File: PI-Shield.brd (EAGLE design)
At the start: 160 x 100 mm, 80 parts, among them IC1 PCF8574T, J10 T2I, J11 T2I, J12 T2I, J13 DF13-4P-1.25DSA, J14 DF13-4P-1.25DSA, J15 DF13-4P-1.25DSA, Q1 220mA/50V/3.5Ω, Q2 220mA/50V/3.5Ω, Q3 220mA/50V/3.5Ω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

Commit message: Board Update
Changes: [Reduced backplane connector from 26->12 positions, added board outline matching last year's, placement of components]
To Do: [Routing, which should be done within next 24 hrs :P]
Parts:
- U$3: value IPL_13X2 -> 6X_CONN; device PI-SHIELD, Solenoid-Backplane:IPL13X2 -> PI-SHIELD, Solenoid-Backplane:IPL6X2
- moved J1 189.3 mm to (67.4, 35.4), turned to 90 degrees
- moved R22 181.9 mm to (34.2, 7.75), turned to 270 degrees
- moved R20 178.4 mm to (46.4, 20.3), flipped to the bottom, turned to 180 degrees
- moved R21 168.4 mm to (17.4, 4.32)
- moved U$8 167.5 mm to (65.9, 3.94), turned to 90 degrees
- moved U3 167.1 mm to (50.5, 10.7), turned to 270 degrees
- moved C10 165.4 mm to (18.0, 12.1), turned to 90 degrees
- moved R15 161.7 mm to (43.8, 18.8), flipped to the bottom
- moved R18 161.6 mm to (17.4, 2.29)
- moved J13 158.7 mm to (61.7, 49.9), turned to 180 degrees
- moved C8 158.3 mm to (21.5, 18.3), flipped to the bottom
- moved C9 157.7 mm to (21.3, 24.5), flipped to the bottom, turned to 180 degrees
- moved J14 157.4 mm to (43.9, 49.9), turned to 180 degrees
- moved R17 155.1 mm to (27.4, 18.5), flipped to the bottom, turned to 180 degrees
- moved R12 153.6 mm to (41.3, 14.7), flipped to the bottom, turned to 90 degrees
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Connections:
- removed net ALERT1: U$3.17
- removed net ALERT2: U$3.19
- removed net C2_1: U$3.21
- removed net C2_2: U$3.22
- removed net DATA: U$3.25
- removed net SWCLK: U$3.11
- removed net SWDIO: U$3.13
- new net N$5: U$3.4
- net +3V3: now also U$3.12; no longer U$3.1
- net 5V: now also U$3.8; no longer U$3.3
- net CAN_H: no longer U$3.24
- net CAN_L: no longer U$3.26
- net CLK: no longer U$3.23
- net GND: now also U$3.10; no longer U$3.15, U$3.20, U$3.4, U$3.5, U$3.7, U$3.9
- net SOL1_1: now also U$3.1; no longer U$3.8
- net SOL2_1: now also U$3.3; no longer U$3.10
- net SOL3_1: now also U$3.5; no longer U$3.12
- net SOL4_1: now also U$3.7; no longer U$3.14
- net SOL5_1: now also U$3.9; no longer U$3.16
- net SOL6_1: now also U$3.11; no longer U$3.18
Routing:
- added copper zone on layer 1, net GND
- added copper zone on layer 16, net GND
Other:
- board size 160 x 100 mm -> 69.8 x 73 mm

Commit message: Schematic Update
Changes: [FREAKING FORGOT TO LABEL A PIN >:((((]
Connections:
- removed net N$5: U$3.4
- net 12V: now also U$3.4
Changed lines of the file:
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@@
 <contactref element="C15" pad="+"/>
 <contactref element="U$3" pad="2"/>
+<contactref element="U$3" pad="4"/>
 <wire x1="46.101" y1="8.193" x2="45.606" y2="18.288" width="0" layer="19" extent="1-1"/>
-<wire x1="44.45" y1="2.667" x2="46.101" y2="8.193" width="0" layer="19" extent="1-1"/>
+<wire x1="46.99" y1="2.667" x2="46.101" y2="8.193" width="0" layer="19" extent="1-1"/>
+<wire x1="44.45" y1="2.667" x2="46.99" y2="2.667" width="0" layer="19" extent="1-1"/>
 </signal>
 <signal name="SOL1_1">
@@
 <wire x1="58.801" y1="19.84" x2="57.15" y2="2.667" width="0" layer="19" extent="16-16"/>
 </signal>
-<signal name="N$5">
-<contactref element="U$3" pad="4"/>
-</signal>
 </signals>

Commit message: Routing Hard >:(
Changes: [Started routing,,,,, it's going well???? i dunno, *power polygons*]
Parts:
- moved U$3 12.5 mm to (50.0, -8.51)
- moved J5 3.82 mm to (67.6, 61.6)
- moved U$6 2.74 mm to (40.0, 2.67)
- moved J7 2.55 mm to (62.7, 38.0), turned to 270 degrees
- moved D1 1.37 mm to (30.7, 43.4)
- moved C12 1.08 mm to (31.0, 39.1)
- moved C4 1.08 mm to (24.9, 43.2)
- moved R1 1.08 mm to (26.5, 43.2)
- moved R10 1.08 mm to (21.5, 40.1)
- moved U2 1.08 mm to (25.3, 37.0)
- moved J1 1.02 mm to (66.4, 35.4)
- moved R2 0.92 mm to (29.0, 43.2), turned to 270 degrees
- moved R5 0.92 mm to (32.3, 70.2)
- moved C11 0.80 mm to (31.0, 35.3)
- moved D4 0.80 mm to (30.2, 17.0)
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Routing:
- net 3V3: track 0.00 -> 142.6 mm, vias 0 -> 2
- net 5V: track 0.00 -> 105.4 mm, vias 0 -> 1
- net CAN_L: track 0.00 -> 43.0 mm, vias 0 -> 1
- net CAN_H: track 0.00 -> 43.0 mm, vias 0 -> 1
- net PWM: track 0.00 -> 41.7 mm
- net PI_POWER: track 0.00 -> 25.8 mm
- net SDA_ADC: track 0.00 -> 17.2 mm
- net AMP_OUT: track 0.00 -> 16.3 mm, vias 0 -> 1
- net CLK: track 0.00 -> 16.2 mm
- net TXCAN: track 0.00 -> 16.1 mm, vias 0 -> 1
- net MISO: track 0.00 -> 15.7 mm
- net INT: track 0.00 -> 15.1 mm
- net RX: track 0.00 -> 14.9 mm
- net TX: track 0.00 -> 14.3 mm
- net RXCAN: track 0.00 -> 14.3 mm, vias 0 -> 1
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- added copper zone on layer 1, net 5V
- added copper zone on layer 1, net 5V_RAW
- added copper zone on layer 1, net PI_POWER

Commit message: Routing :)
Change: [bro why this game of flow so hard??]
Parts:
- moved C15 23.7 mm to (65.5, 34.3), turned to 270 degrees
- moved U$3 19.1 mm to (58.2, 8.76), turned to 180 degrees
- moved U3 15.1 mm to (62.0, 20.6), flipped to the bottom, turned to 180 degrees
- moved R20 8.62 mm to (48.4, 28.7)
- moved R9 8.07 mm to (46.6, 31.0)
- moved R8 8.02 mm to (48.3, 33.4)
- moved C13 7.58 mm to (45.0, 37.8)
- moved J6 7.55 mm to (40.8, 56.5), turned to 180 degrees
- moved J1 7.37 mm to (66.4, 42.8)
- moved J7 7.37 mm to (62.7, 45.3)
- moved R12 4.34 mm to (45.5, 15.9), turned to 0 degrees
- moved U$6 3.61 mm to (37.7, 5.46), turned to 90 degrees
- moved U$4 3.45 mm to (35.3, 47.8)
- moved U$5 3.45 mm to (40.5, 47.1)
- moved IC1 3.41 mm to (57.4, 16.8), flipped to the top, turned to 90 degrees
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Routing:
- net SDA: track 13.4 -> 137.7 mm, vias 0 -> 7
- net SCL: track 12.9 -> 130.3 mm, vias 0 -> 6
- net A_INT: track 0.00 -> 66.6 mm
- net 5V: track 105.4 -> 168.0 mm, vias 1 -> 4
- net 3V3: track 142.6 -> 201.6 mm, vias 2 -> 3
- net !AMP_RESET: track 0.00 -> 53.1 mm, vias 0 -> 1
- net IMU_INT: track 7.53 -> 59.5 mm, vias 0 -> 1
- net SOL6_1: track 0.00 -> 47.8 mm
- net SOL5_1: track 0.00 -> 42.0 mm
- net 12V: track 0.00 -> 37.8 mm, vias 0 -> 1
- net SOL4_1: track 0.00 -> 37.3 mm
- net SOL3_1: track 0.00 -> 31.8 mm
- net IMU_RESET: track 0.00 -> 30.9 mm
- net SOL2_1: track 0.00 -> 26.9 mm
- net MOSI: track 13.7 -> 37.2 mm
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
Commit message: Fixed Like 2 Routes smh
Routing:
- net SCL: track 130.3 -> 137.4 mm
- net SDA: track 137.7 -> 142.7 mm
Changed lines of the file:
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@@
 <layer number="43" name="vRestrict" color="2" fill="10" visible="yes" active="yes"/>
 <layer number="44" name="Drills" color="7" fill="1" visible="no" active="yes"/>
-<layer number="45" name="Holes" color="7" fill="1" visible="no" active="yes"/>
+<layer number="45" name="Holes" color="7" fill="1" visible="yes" active="yes"/>
 <layer number="46" name="Milling" color="3" fill="1" visible="no" active="yes"/>
 <layer number="47" name="Measures" color="7" fill="1" visible="no" active="yes"/>
@@
 <wire x1="61.468" y1="47.498" x2="66.04" y2="47.498" width="0.254" layer="16"/>
 <wire x1="66.04" y1="47.498" x2="66.421" y2="47.879" width="0.254" layer="16"/>
-<wire x1="50.546" y1="41.91" x2="49.022" y2="40.386" width="0.254" layer="1"/>
+<wire x1="50.038" y1="41.402" x2="49.022" y2="40.386" width="0.254" layer="1"/>
 <wire x1="49.022" y1="40.386" x2="49.022" y2="39.624" width="0.254" layer="1"/>
 <via x="49.022" y="39.624" extent="1-16" drill="0.35"/>
 <wire x1="49.022" y1="39.624" x2="49.022" y2="33.489" width="0.254" layer="16"/>
 <wire x1="49.022" y1="33.489" x2="49.11" y2="33.401" width="0.254" layer="16"/>
-<wire x1="50.546" y1="45.212" x2="45.847" y2="49.911" width="0.254" layer="1"/>
-<wire x1="43.805" y1="49.911" x2="45.847" y2="49.911" width="0.254" layer="1"/>
-<wire x1="50.546" y1="45.212" x2="50.546" y2="41.91" width="0.254" layer="1"/>
+<wire x1="43.805" y1="49.911" x2="43.805" y2="49.159" width="0.254" layer="1"/>
+<wire x1="50.038" y1="42.926" x2="43.805" y2="49.159" width="0.254" layer="1"/>
+<wire x1="50.038" y1="42.926" x2="50.038" y2="41.402" width="0.254" layer="1"/>
 <wire x1="14.1732" y1="14.8336" x2="15.3416" y2="14.8336" width="0.254" layer="1"/>
 <wire x1="15.3416" y1="14.8336" x2="18.796" y2="18.288" width="0.254" layer="1"/>
@@
 <wire x1="41.574" y1="13.97" x2="42.926" y2="13.97" width="0.254" layer="16"/>
 <via x="42.926" y="13.97" extent="1-16" drill="0.35"/>
-<wire x1="45.72" y1="13.462" x2="43.434" y2="13.462" width="0.254" layer="1"/>
+<wire x1="43.434" y1="13.462" x2="45.72" y2="13.462" width="0.254" layer="1"/>
 <wire x1="42.926" y1="13.97" x2="43.434" y2="13.462" width="0.254" layer="1"/>
-<wire x1="45.72" y1="13.462" x2="45.974" y2="13.716" width="0.254" layer="1"/>
-<via x="45.974" y="13.716" extent="1-16" drill="0.35"/>
 <wire x1="46.482" y1="15.709" x2="46.482" y2="14.224" width="0.254" layer="16"/>
-<wire x1="45.974" y1="13.716" x2="46.482" y2="14.224" width="0.254" layer="16"/>
 <wire x1="46.316" y1="15.875" x2="46.482" y2="15.709" width="0.254" layer="16"/>
-<wire x1="45.974" y1="13.716" x2="52.804" y2="13.589" width="0" layer="19" extent="1-1"/>
+<wire x1="52.804" y1="13.589" x2="47.117" y2="13.589" width="0.254" layer="1"/>
+<wire x1="47.117" y1="13.589" x2="46.482" y2="14.224" width="0.254" layer="1"/>
+<via x="46.482" y="14.224" extent="1-16" drill="0.35"/>
+<wire x1="45.72" y1="13.462" x2="46.482" y2="14.224" width="0.254" layer="1"/>
 </signal>
 <signal name="SCL">
@@
 <wire x1="46.228" y1="36.83" x2="46.228" y2="36.322" width="0.254" layer="1"/>
 <via x="46.228" y="36.322" extent="1-16" drill="0.35"/>
-<wire x1="47.752" y1="45.72" x2="43.561" y2="49.911" width="0.254" layer="1"/>
-<wire x1="42.555" y1="49.911" x2="43.561" y2="49.911" width="0.254" layer="1"/>
-<wire x1="47.752" y1="45.72" x2="47.752" y2="38.354" width="0.254" layer="1"/>
+<wire x1="47.752" y1="43.434" x2="42.555" y2="48.631" width="0.254" layer="1"/>
+<wire x1="42.555" y1="49.911" x2="42.555" y2="48.631" width="0.254" layer="1"/>
+<wire x1="47.752" y1="43.434" x2="47.752" y2="38.354" width="0.254" layer="1"/>
 <wire x1="46.228" y1="34.544" x2="45.72" y2="34.036" width="0.254" layer="16"/>
 <wire x1="45.72" y1="34.036" x2="45.72" y2="31.027" width="0.254" layer="16"/>
@@
 <wire x1="46.228" y1="17.526" x2="46.4625" y2="17.7605" width="0.254" layer="16"/>
 <wire x1="46.4625" y1="17.7605" x2="46.4625" y2="19.5775" width="0.254" layer="16"/>
-<wire x1="46.228" y1="17.526" x2="52.804" y2="14.859" width="0" layer="19" extent="1-1"/>
+<wire x1="46.228" y1="17.526" x2="47.498" y2="17.526" width="0.254" layer="1"/>
+<wire x1="50.165" y1="14.859" x2="52.804" y2="14.859" width="0.254" layer="1"/>
+<wire x1="47.498" y1="17.526" x2="50.165" y2="14.859" width="0.254" layer="1"/>
 <wire x1="41.91" y1="29.972" x2="41.783" y2="29.972" width="0" layer="19" extent="16-16"/>
 </signal>

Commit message: Update PI-Shield.brd
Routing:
- net 5V: track 168.0 -> 171.4 mm, vias 4 -> 5
- net PI_POWER: track 25.8 -> 27.1 mm
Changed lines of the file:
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@@
 <wire x1="34.544" y1="9.906" x2="34.036" y2="9.906" width="0.635" layer="1"/>
 <wire x1="47.244" y1="6.223" x2="36.703" y2="6.223" width="0.635" layer="1"/>
+<via x="27.94" y="12.954" extent="1-16" drill="0.35"/>
+<wire x1="25.9748" y1="15.428" x2="26.9644" y2="14.4384" width="0.508" layer="16"/>
+<wire x1="26.9644" y1="14.4384" x2="26.9644" y2="13.6556625" width="0.508" layer="16"/>
+<wire x1="27.94" y1="12.954" x2="27.6660625" y2="12.954" width="0.508" layer="16"/>
+<wire x1="27.6660625" y1="12.954" x2="26.9644" y2="13.6556625" width="0.508" layer="16"/>
 <wire x1="18.249" y1="2.286" x2="18.288" y2="1.4732" width="0" layer="19" extent="1-16"/>
-<wire x1="25.8748" y1="15.328" x2="26.924" y2="11.684" width="0" layer="19" extent="1-16"/>
 </signal>
 <signal name="RX0_INT">
@@
 <wire x1="8.1846" y1="8.845" x2="11.6332" y2="12.2936" width="1.778" layer="1"/>
 <wire x1="11.6332" y1="12.2936" x2="11.6332" y2="14.8336" width="1.778" layer="1"/>
-<wire x1="4.191" y1="8.845" x2="9.734" y2="3.302" width="1.778" layer="1"/>
-<wire x1="9.734" y1="3.302" x2="14.224" y2="3.302" width="1.778" layer="1"/>
+<wire x1="7.448" y1="3.302" x2="4.191" y2="6.559" width="1.778" layer="1"/>
+<wire x1="4.191" y1="8.845" x2="4.191" y2="6.559" width="1.778" layer="1"/>
+<wire x1="7.448" y1="3.302" x2="14.224" y2="3.302" width="1.778" layer="1"/>
 <polygon width="0.1524" layer="1">
 <vertex x="13.97" y="5.334"/>
@@
 <wire x1="57.023" y1="4.064" x2="62.8396" y2="4.064" width="0.3048" layer="16"/>
 <wire x1="62.8396" y1="4.064" x2="65.786" y2="7.0104" width="0.3048" layer="16"/>
-<wire x1="65.786" y1="7.0104" x2="65.786" y2="15.748" width="0.3048" layer="16"/>
-<wire x1="65.786" y1="15.748" x2="65.405" y2="16.129" width="0.3048" layer="16"/>
-<wire x1="65.405" y1="16.129" x2="64.451" y2="16.129" width="0.3048" layer="16"/>
+<wire x1="65.786" y1="7.0104" x2="65.786" y2="15.494" width="0.3048" layer="16"/>
+<wire x1="65.786" y1="15.494" x2="65.151" y2="16.129" width="0.3048" layer="16"/>
+<wire x1="65.151" y1="16.129" x2="64.451" y2="16.129" width="0.3048" layer="16"/>
 </signal>
 <signal name="SOL2_1">

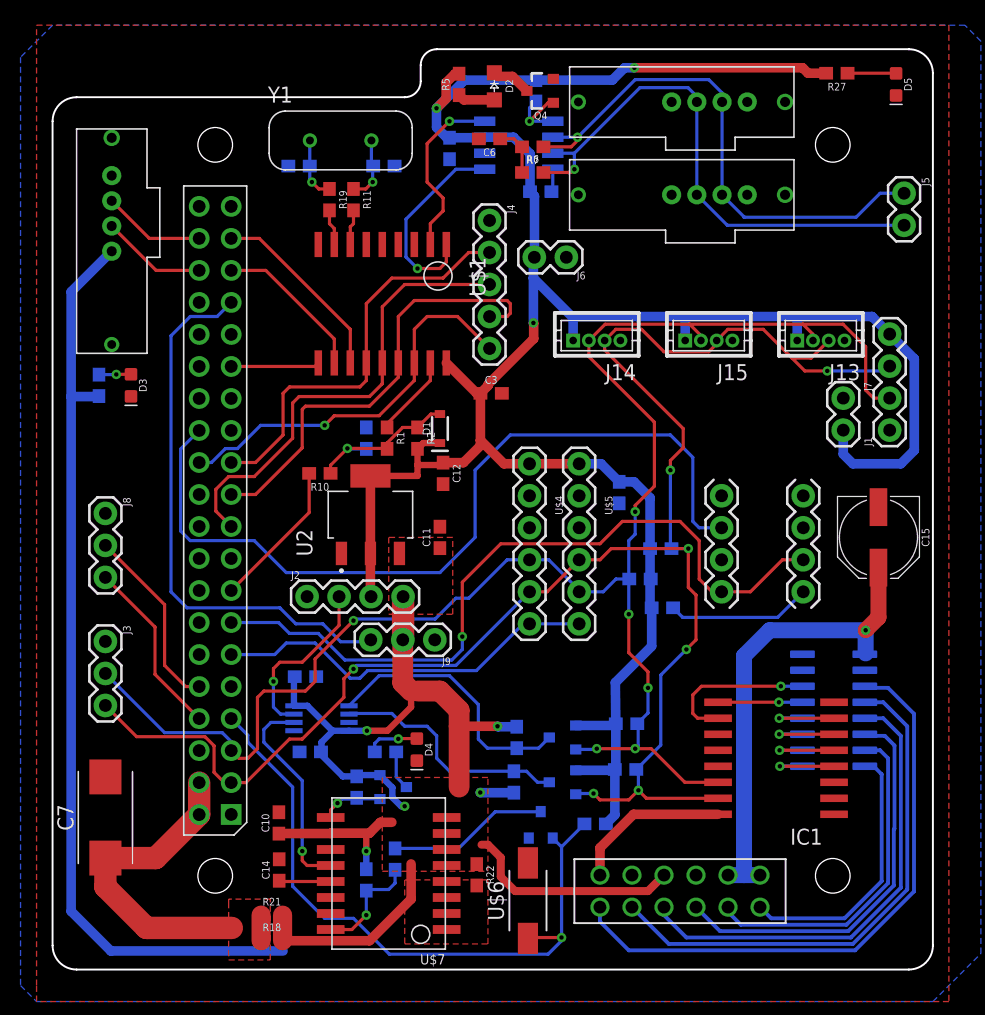
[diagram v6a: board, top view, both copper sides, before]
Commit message: Alumni Design Updates
Changes: [Trace Matched SCL/SDA & TX/RX, added alumni feedback]
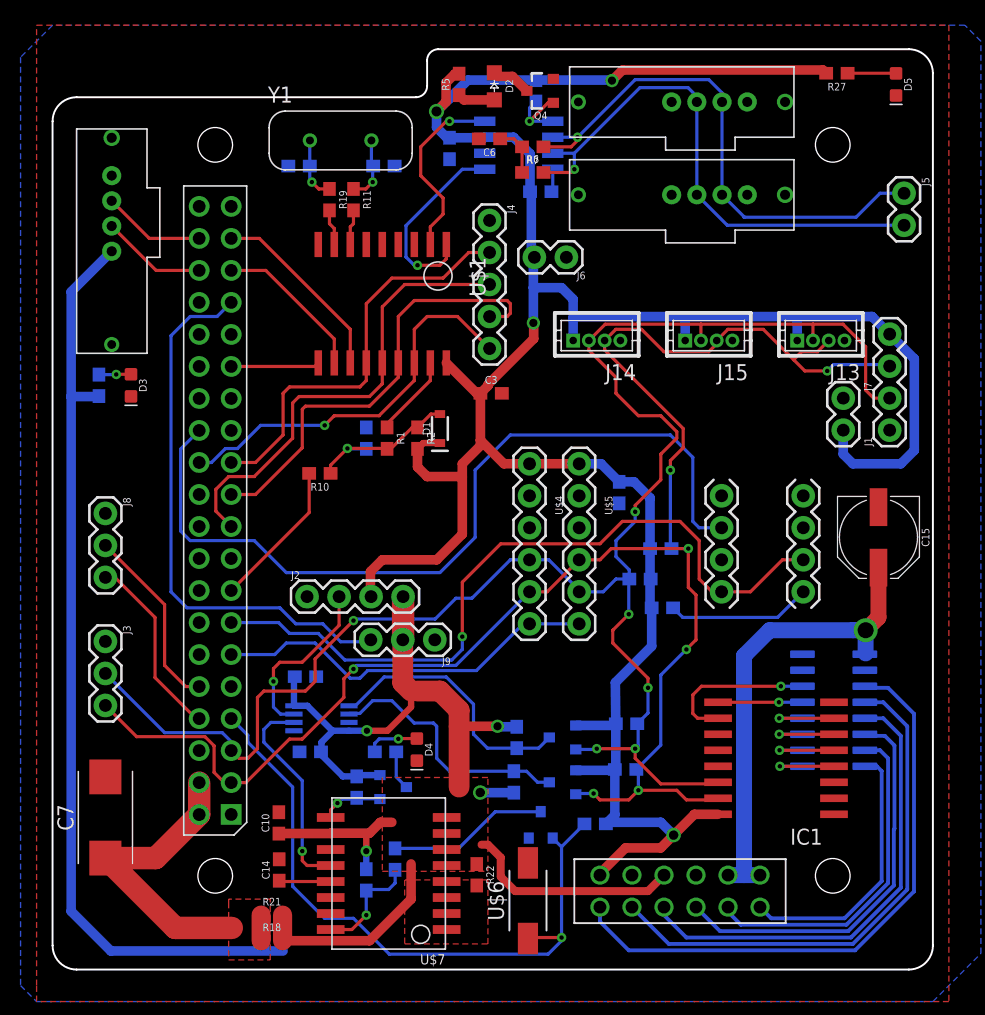
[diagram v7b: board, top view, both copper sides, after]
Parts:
- removed C11, C12: 4.7uF, SparkFun-Capacitors:0603
- removed U2: AZ1117EH-3.3TRG1, AZ1117EH-3.3TRG1:SOT230P700X180-4N
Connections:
- removed net +3V3: IC1.16, U$3.12
- net 3V3: now also IC1.16, U$3.12; no longer C12.1, U2.2, U2.4
- net 5V: no longer C11.1, U2.3
- net GND: no longer C11.2, C12.2, U2.1
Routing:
- net 3V3: track 201.6 -> 221.7 mm, vias 3 -> 4
- net +3V3: track 12.6 -> 0.00 mm
- net SCL: track 137.4 -> 142.7 mm
- net 5V: track 171.4 -> 168.0 mm, vias 5 -> 4
- net PI_POWER: track 27.1 -> 25.8 mm
- net SDA_ADC: track 19.8 -> 21.1 mm
- net RXCAN: track 14.3 -> 15.2 mm
- net TXCAN: track 16.1 -> 15.4 mm
- net TX: track 14.3 -> 14.9 mm
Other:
- outline, holes or cut-outs redrawn

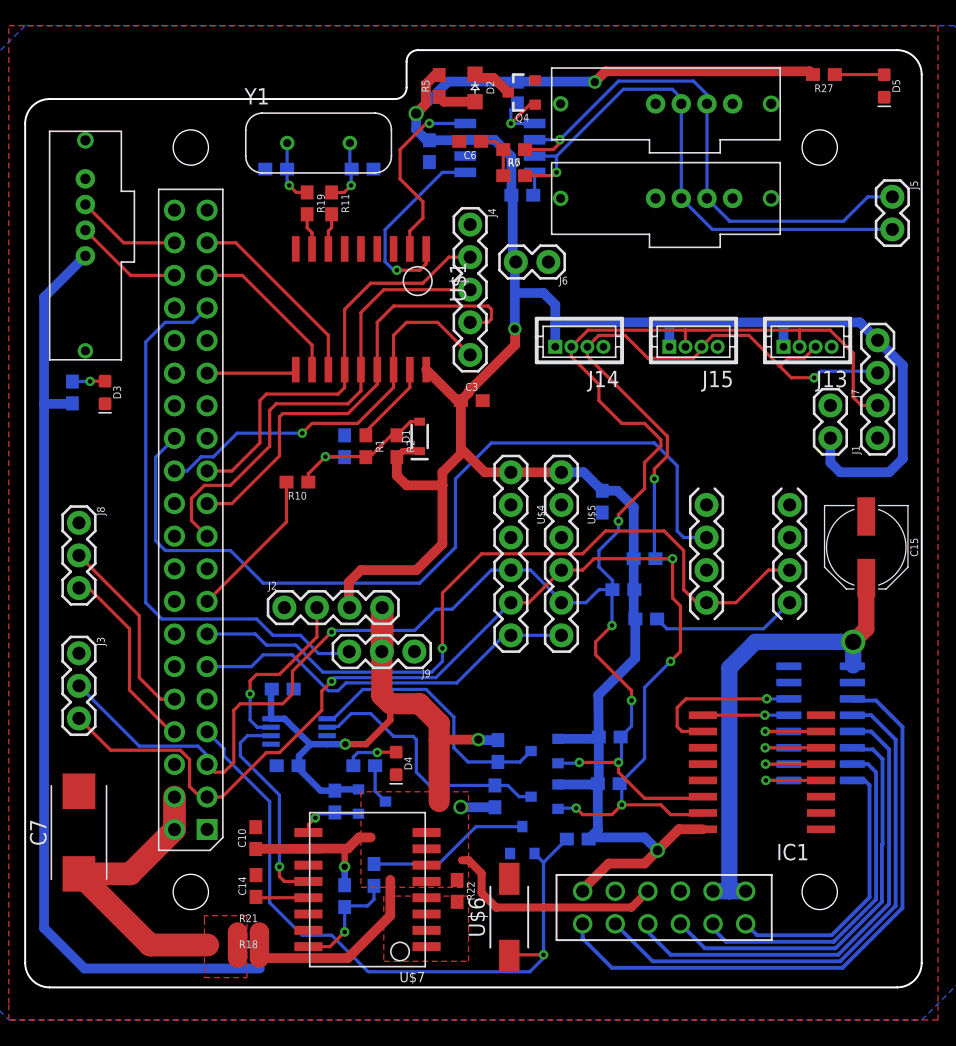
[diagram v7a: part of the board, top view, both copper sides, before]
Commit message: Update PI-Shield.brd
fixed errors
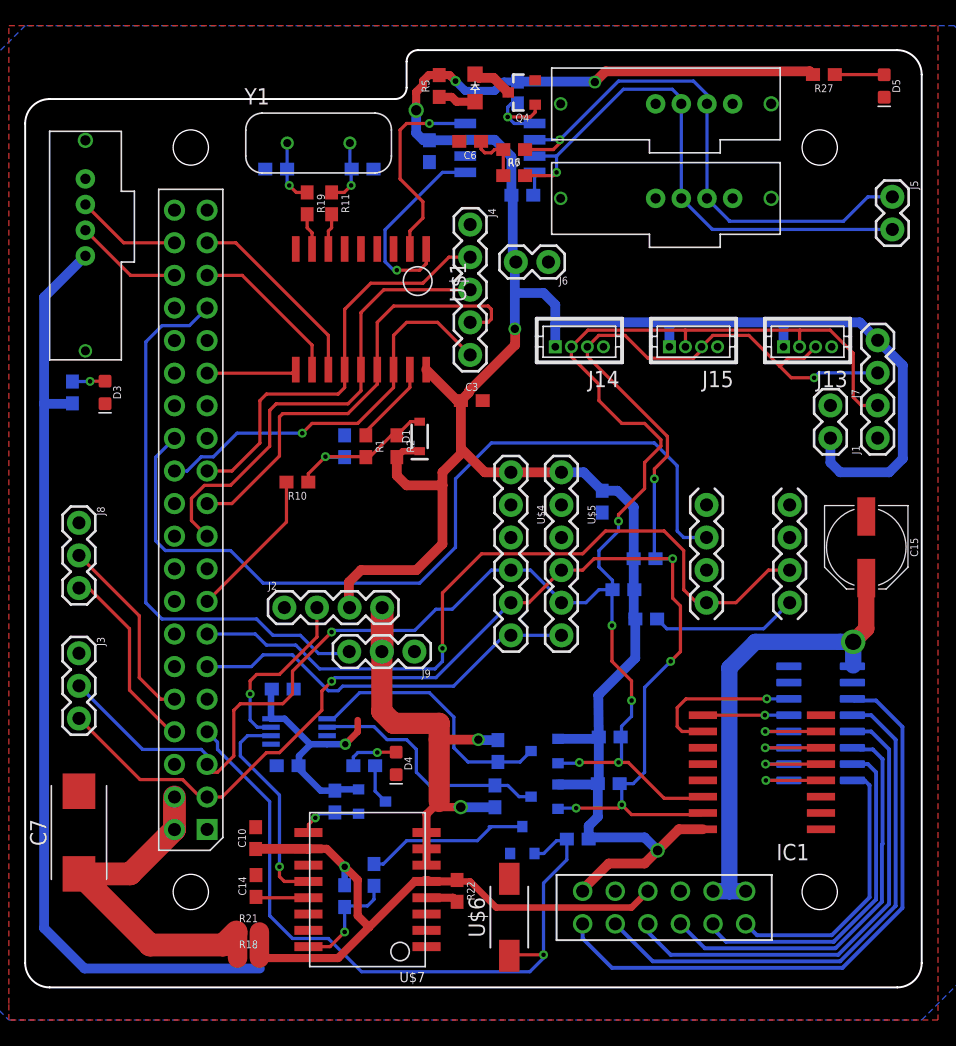
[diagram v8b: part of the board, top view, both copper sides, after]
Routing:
- net 5V: track 168.0 -> 177.8 mm
- net PI_POWER: track 25.8 -> 28.4 mm
- net !AMP_RESET: track 53.1 -> 55.6 mm
- net 5V_RAW: track 0.00 -> 2.52 mm
- net SDA_ADC: track 21.1 -> 19.2 mm
- net 3V3: track 221.7 -> 219.9 mm, vias 4 -> 5
- net SCL: track 142.7 -> 141.0 mm
- net SDA: track 142.8 -> 141.7 mm
- net FAULT: track 6.11 -> 6.84 mm
- net CAN_TERM_COM: track 4.02 -> 4.69 mm
- net RXCAN: track 15.2 -> 15.7 mm
- removed copper zone on layer 1, net 5V
- removed copper zone on layer 1, net 5V_RAW
- removed copper zone on layer 1, net PI_POWER
